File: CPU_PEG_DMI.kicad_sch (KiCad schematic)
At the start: 1 part

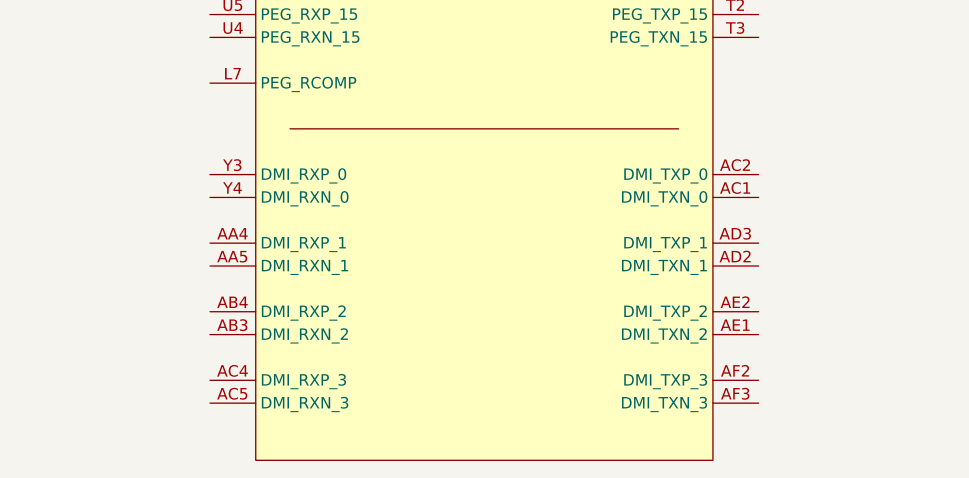
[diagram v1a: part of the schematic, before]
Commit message: Connected DMI for fun (with lane reversal)
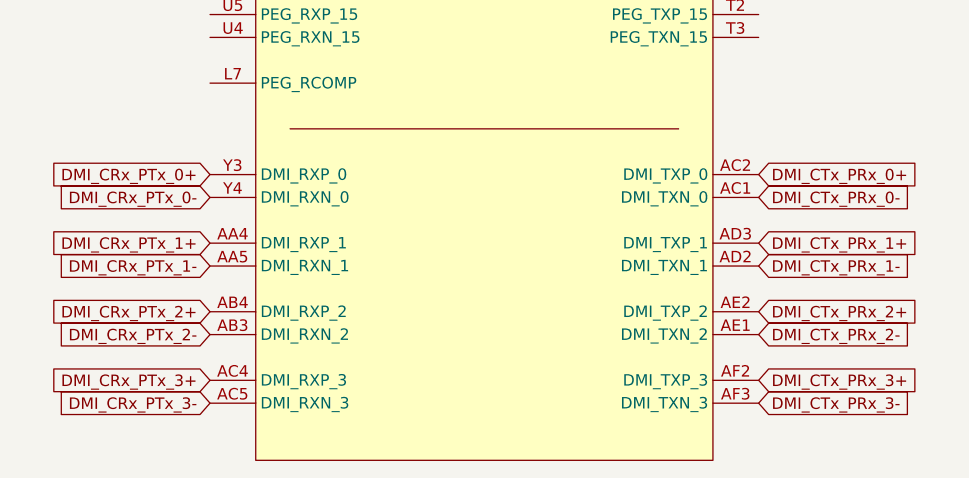
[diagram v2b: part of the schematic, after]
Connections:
- net DMI_CRx_PTx_1+: now reaches JCPU1.AA4 (DMI_RXP_1)
- net DMI_CRx_PTx_1-: now reaches JCPU1.AA5 (DMI_RXN_1)
- net DMI_CRx_PTx_2-: now reaches JCPU1.AB3 (DMI_RXN_2)
- net DMI_CRx_PTx_2+: now reaches JCPU1.AB4 (DMI_RXP_2)
- net DMI_CTx_PRx_0-: now reaches JCPU1.AC1 (DMI_TXN_0)
- net DMI_CTx_PRx_0+: now reaches JCPU1.AC2 (DMI_TXP_0)
- net DMI_CRx_PTx_3+: now reaches JCPU1.AC4 (DMI_RXP_3)
- net DMI_CRx_PTx_3-: now reaches JCPU1.AC5 (DMI_RXN_3)
- net DMI_CTx_PRx_1-: now reaches JCPU1.AD2 (DMI_TXN_1)
- net DMI_CTx_PRx_1+: now reaches JCPU1.AD3 (DMI_TXP_1)
- net DMI_CTx_PRx_2-: now reaches JCPU1.AE1 (DMI_TXN_2)
- net DMI_CTx_PRx_2+: now reaches JCPU1.AE2 (DMI_TXP_2)
- net DMI_CTx_PRx_3+: now reaches JCPU1.AF2 (DMI_TXP_3)
- net DMI_CTx_PRx_3-: now reaches JCPU1.AF3 (DMI_TXN_3)
- net DMI_CRx_PTx_0+: now reaches JCPU1.Y3 (DMI_RXP_0)
- net DMI_CRx_PTx_0-: now reaches JCPU1.Y4 (DMI_RXN_0)
